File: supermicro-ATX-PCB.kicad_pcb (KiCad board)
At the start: 2 copper layers, 27.9 x 30.5 mm, 6 parts

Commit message: added through hole for female header
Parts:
- removed ATX-FP: Conn_02x05_Odd_Even, Connector_PinSocket_2.54mm:PinSocket_2x05_P2.54mm_Vertical
- added ATX-FP1: Conn_02x05_Odd_Even, Connector_PinSocket_2.54mm:PinSocket_2x05_P2.54mm_Vertical, B.Cu at (104.1, 78.7)
- moved PWR_FAIL 0.38 mm to (122.6, 63.5)
- moved UID 0.38 mm to (122.6, 68.6)
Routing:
- net /PWR_LED+: track 11.2 -> 13.1 mm

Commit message: testing SMD Female
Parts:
- removed PWR_FAIL, UID: Conn_01x02_Pin, Connector_PinHeader_2.54mm:PinHeader_2x01_P2.54mm_Vertical
- added PWR_FAIL1: Conn_01x02_Pin, Connector_PinHeader_2.54mm:PinHeader_2x01_P2.54mm_Vertical, F.Cu at (123.2, 63.5)
- added UID1: Conn_01x02_Pin, Connector_PinHeader_2.54mm:PinHeader_2x01_P2.54mm_Vertical, F.Cu at (123.2, 68.6)
- ATX-FP1: footprint Connector_PinSocket_2.54mm:PinSocket_2x05_P2.54mm_Vertical -> Connector_PinSocket_2.54mm:PinSocket_2x05_P2.54mm_Vertical_SMD
- moved ATX-FP1 5.69 mm to (101.6, 73.7)
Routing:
- net /PWR_BUTT: track 16.3 -> 1.66 mm
- net GND: track 13.8 -> 0.00 mm
- net /PWR_LED+: track 13.1 -> 0.00 mm
- net /RESET_BUTT: track 11.7 -> 0.00 mm
- net /PWR_LED-: track 11.1 -> 0.00 mm
- net /HDD_LED+: track 8.57 -> 0.00 mm
- net /HDD_LED-: track 6.13 -> 0.00 mm
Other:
- board size 27.9 x 30.5 mm -> 29.3 x 30.5 mm

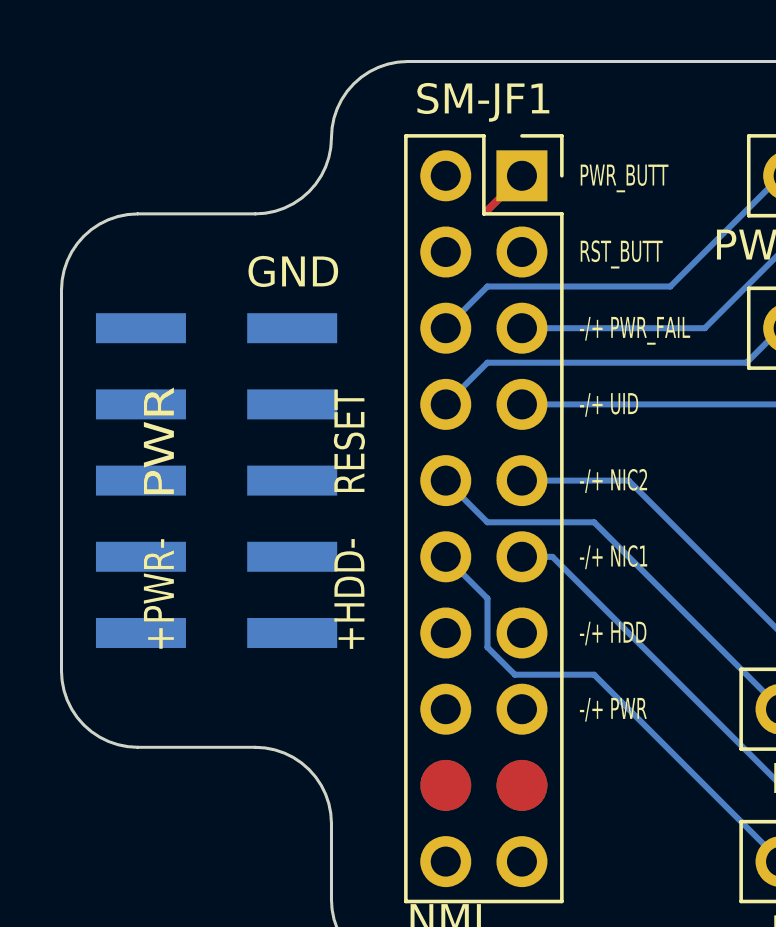
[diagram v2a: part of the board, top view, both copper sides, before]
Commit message: added routing for SMT ATX Female
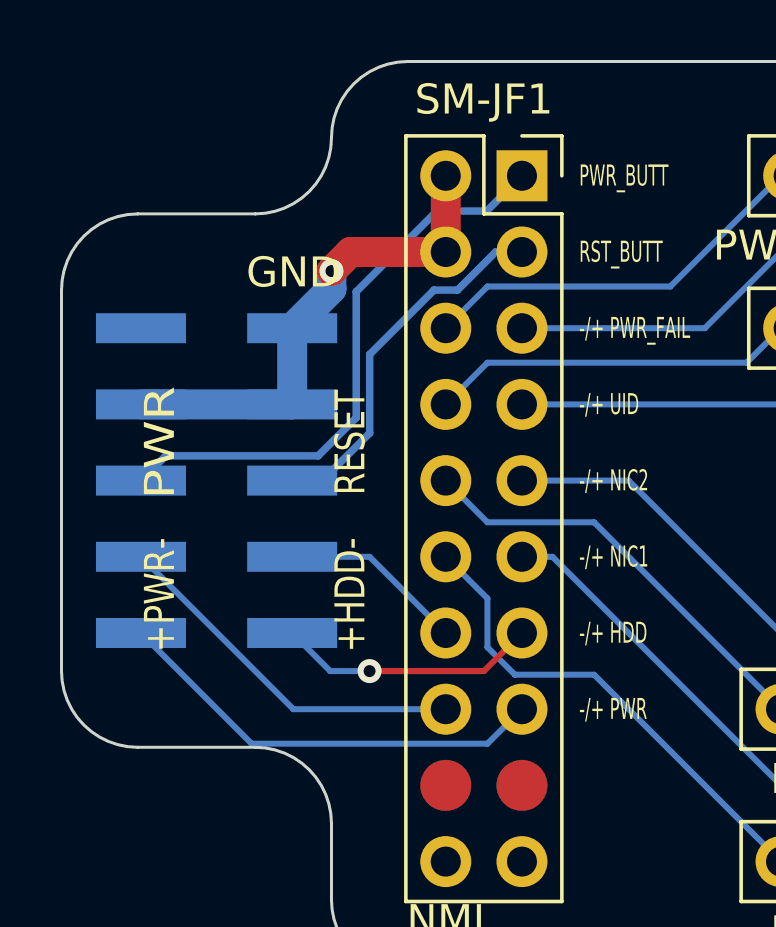
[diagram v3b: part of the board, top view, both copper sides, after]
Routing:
- net /PWR_BUTT: track 1.66 -> 19.4 mm
- net GND: track 0.00 -> 16.6 mm, vias 0 -> 1
- net /PWR_LED+: track 0.00 -> 14.7 mm
- net /RESET_BUTT: track 0.00 -> 12.4 mm
- net /PWR_LED-: track 0.00 -> 12.3 mm
- net /HDD_LED+: track 0.00 -> 8.71 mm, vias 0 -> 1
- net /HDD_LED-: track 0.00 -> 6.17 mm
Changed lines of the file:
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@@
     (effects (font (size 0.7 0.4) (thickness 0.1)) (justify left))
   )
-  (segment (start 111.76 63.5) (end 110.585 64.675) (width 0.25) (layer "F.Cu") (net 6))
+  (segment (start 106.68 80.01) (end 110.49 80.01) (width 0.2) (layer "F.Cu") (net 1))
+  (segment (start 110.49 80.01) (end 111.76 78.74) (width 0.2) (layer "F.Cu") (net 1))
+  (via (at 106.68 80.01) (size 0.8) (drill 0.4) (layers "F.Cu" "B.Cu") (net 1))
+  (segment (start 104.1 78.74) (end 105.37 80.01) (width 0.2) (layer "B.Cu") (net 1))
+  (segment (start 105.37 80.01) (end 106.68 80.01) (width 0.2) (layer "B.Cu") (net 1))
+  (segment (start 110.61 82.43) (end 102.75 82.43) (width 0.2) (layer "B.Cu") (net 2))
+  (segment (start 111.76 81.28) (end 110.61 82.43) (width 0.2) (layer "B.Cu") (net 2))
+  (segment (start 102.75 82.43) (end 99.06 78.74) (width 0.2) (layer "B.Cu") (net 2))
+  (segment (start 104.1 76.2) (end 106.68 76.2) (width 0.2) (layer "B.Cu") (net 3))
+  (segment (start 106.68 76.2) (end 109.22 78.74) (width 0.2) (layer "B.Cu") (net 3))
+  (segment (start 104.14 81.28) (end 99.06 76.2) (width 0.2) (layer "B.Cu") (net 4))
+  (segment (start 109.22 81.28) (end 104.14 81.28) (width 0.2) (layer "B.Cu") (net 4))
+  (segment (start 111.76 66.04) (end 110.881701 66.04) (width 0.25) (layer "B.Cu") (net 5))
+  (segment (start 105.1 73.66) (end 104.1 73.66) (width 0.25) (layer "B.Cu") (net 5))
+  (segment (start 109.611701 67.31) (end 108.828299 67.31) (width 0.25) (layer "B.Cu") (net 5))
+  (segment (start 106.685 69.453299) (end 106.685 72.075) (width 0.25) (layer "B.Cu") (net 5))
+  (segment (start 108.828299 67.31) (end 106.685 69.453299) (width 0.25) (layer "B.Cu") (net 5))
+  (segment (start 106.685 72.075) (end 105.1 73.66) (width 0.25) (layer "B.Cu") (net 5))
+  (segment (start 110.881701 66.04) (end 109.611701 67.31) (width 0.25) (layer "B.Cu") (net 5))
+  (segment (start 104.965 72.835) (end 99.885 72.835) (width 0.25) (layer "B.Cu") (net 6))
+  (segment (start 108.923299 64.675) (end 106.235 67.363299) (width 0.25) (layer "B.Cu") (net 6))
+  (segment (start 110.585 64.675) (end 108.923299 64.675) (width 0.25) (layer "B.Cu") (net 6))
+  (segment (start 106.235 67.363299) (end 106.235 71.565) (width 0.25) (layer "B.Cu") (net 6))
+  (segment (start 99.885 72.835) (end 99.06 73.66) (width 0.25) (layer "B.Cu") (net 6))
+  (segment (start 106.235 71.565) (end 104.965 72.835) (width 0.25) (layer "B.Cu") (net 6))
+  (segment (start 111.76 63.5) (end 110.585 64.675) (width 0.25) (layer "B.Cu") (net 6))
+  (segment (start 109.22 63.5) (end 109.22 66.04) (width 1) (layer "F.Cu") (net 7))
+  (segment (start 106.045 66.04) (end 105.41 66.675) (width 1) (layer "F.Cu") (net 7))
+  (segment (start 109.22 66.04) (end 106.045 66.04) (width 1) (layer "F.Cu") (net 7))
+  (via (at 105.41 66.675) (size 0.8) (drill 0.4) (layers "F.Cu" "B.Cu") (net 7))
+  (segment (start 104.1 71.12) (end 99.06 71.12) (width 1) (layer "B.Cu") (net 7))
+  (segment (start 104.1 68.58) (end 104.1 71.12) (width 1) (layer "B.Cu") (net 7))
+  (segment (start 105.41 67.27) (end 104.1 68.58) (width 1) (layer "B.Cu") (net 7))
+  (segment (start 105.41 66.675) (end 105.41 67.27) (width 1) (layer "B.Cu") (net 7))
   (segment (start 120.396 86.36) (end 114.166 80.13) (width 0.2) (layer "B.Cu") (net 9))
   (segment (start 110.61 79.216346) (end 110.61 77.59) (width 0.2) (layer "B.Cu") (net 9))

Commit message: added THT board
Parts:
- removed PWR_FAIL1, UID1: Conn_01x02_Pin, Connector_PinHeader_2.54mm:PinHeader_2x01_P2.54mm_Vertical
- added PWR_FAIL: Conn_01x02_Pin, Connector_PinHeader_2.54mm:PinHeader_2x01_P2.54mm_Vertical, F.Cu at (122.9, 63.5)
- added UID: Conn_01x02_Pin, Connector_PinHeader_2.54mm:PinHeader_2x01_P2.54mm_Vertical, F.Cu at (122.9, 68.6)
- ATX-FP1: footprint Connector_PinSocket_2.54mm:PinSocket_2x05_P2.54mm_Vertical_SMD -> Connector_PinSocket_2.54mm:PinSocket_2x05_P2.54mm_Vertical
- moved ATX-FP1 5.69 mm to (104.1, 78.7)
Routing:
- net /PWR_BUTT: track 19.4 -> 16.3 mm
- net GND: track 16.6 -> 13.8 mm, vias 1 -> 0
- net /PWR_LED+: track 14.7 -> 13.1 mm
- net /PWR_LED-: track 12.3 -> 11.1 mm
- net /RESET_BUTT: track 12.4 -> 11.7 mm
- net /HDD_LED+: track 8.71 -> 8.57 mm, vias 1 -> 0
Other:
- board size 29.3 x 30.5 mm -> 27.9 x 30.5 mm

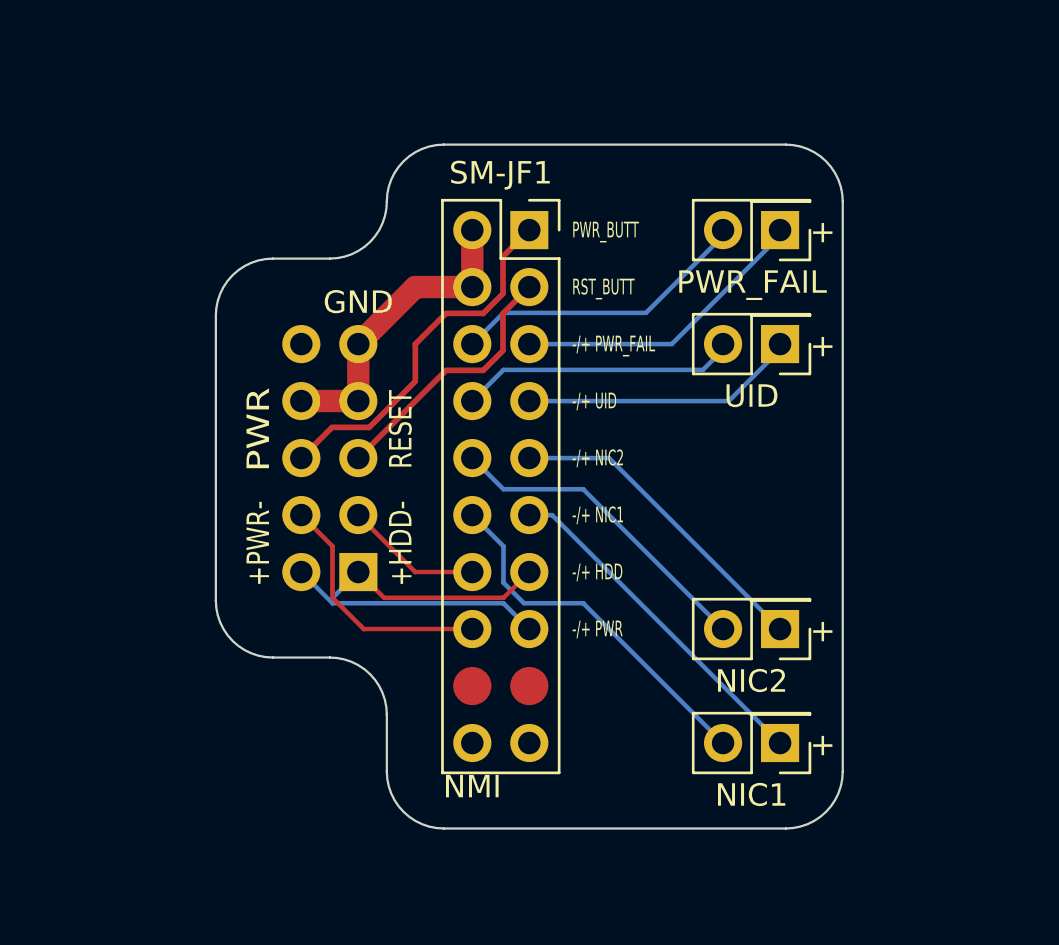
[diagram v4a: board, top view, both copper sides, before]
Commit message: switched polarity of LEDs, isolated all terminals of buttons
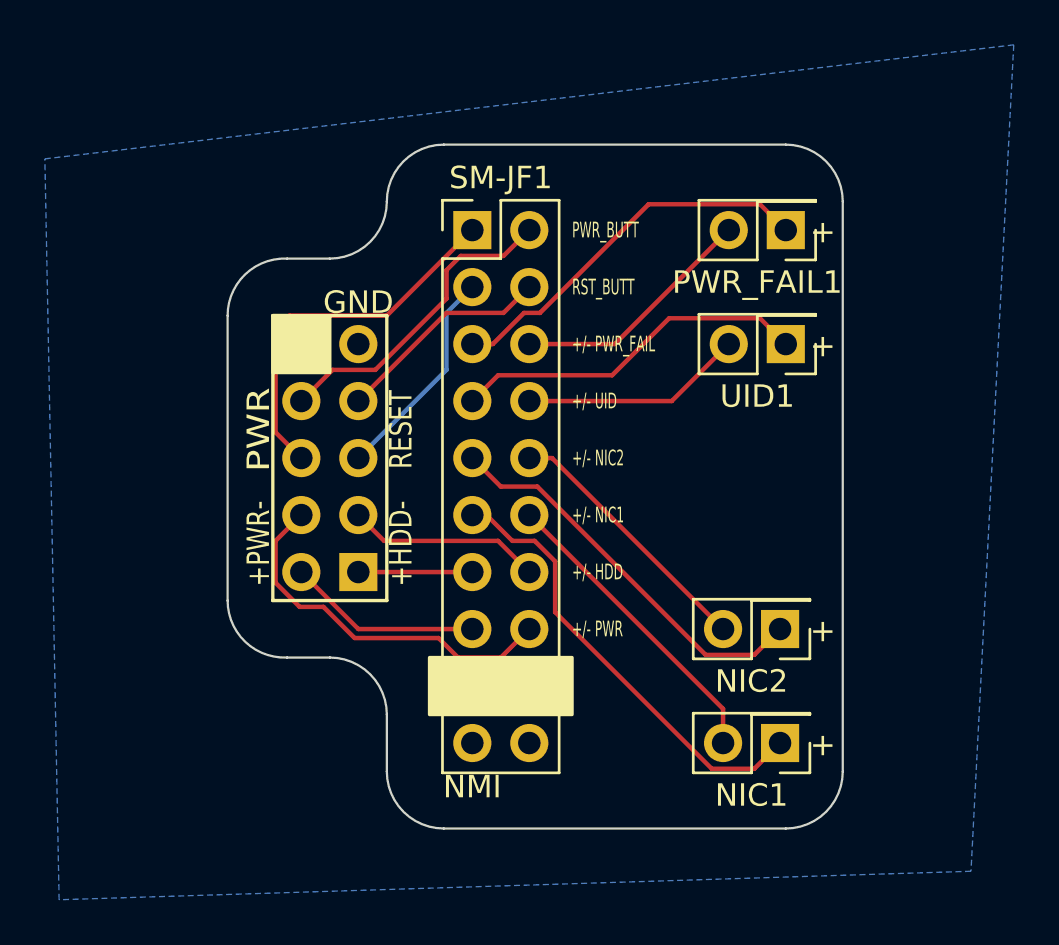
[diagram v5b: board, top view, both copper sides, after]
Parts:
- removed PWR_FAIL, UID: Conn_01x02_Pin, Connector_PinHeader_2.54mm:PinHeader_2x01_P2.54mm_Vertical
- added PWR_FAIL1: Conn_01x02_Pin, Connector_PinHeader_2.54mm:PinHeader_2x01_P2.54mm_Vertical, F.Cu at (123.2, 63.5)
- added UID1: Conn_01x02_Pin, Connector_PinHeader_2.54mm:PinHeader_2x01_P2.54mm_Vertical, F.Cu at (123.2, 68.6)
- SM-JF1: footprint Connector_PinSocket_2.54mm:PinSocket_2x10_P2.54mm_Vertical -> Connector_PinHeader_2.54mm:PinHeader_2x10_P2.54mm_Vertical
- moved SM-JF1 2.54 mm to (109.2, 63.5)
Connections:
- net /PWR_BUTT renamed /PWR_BUTT+
- net /RESET_BUTT renamed /RESET_BUTT+
- ATX-FP1 pad 7: GND -> /RESET_BUTT-
- ATX-FP1 pad 8: GND -> /PWR_BUTT-
- SM-JF1 pad 2: GND -> /PWR_BUTT-
- SM-JF1 pad 4: GND -> /RESET_BUTT-
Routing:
- net /PWR_BUTT-: track 0.00 -> 14.1 mm
- net GND: track 13.8 -> 0.00 mm
- net /RESET_BUTT-: track 0.00 -> 9.72 mm
- net /PWR_LED-: track 11.1 -> 16.7 mm
- net /NIC1_LED+: track 15.4 -> 20.2 mm
- net /PWR_LED+: track 13.1 -> 8.67 mm
- net /NIC2_LED+: track 14.3 -> 17.8 mm
- net /HDD_LED+: track 8.57 -> 5.08 mm
- net /PWR_FAIL_LED+: track 13.5 -> 17.0 mm
- net /UID_LED+: track 12.5 -> 16.0 mm
- net /NIC1_LED-: track 16.3 -> 13.7 mm
- net /UID_LED-: track 12.5 -> 9.94 mm
- net /PWR_FAIL_LED-: track 13.5 -> 11.0 mm
- net /NIC2_LED-: track 14.3 -> 11.8 mm
- net /HDD_LED-: track 6.13 -> 8.67 mm
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- added copper zone on B.Cu, net GND
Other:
- board size 27.9 x 30.5 mm -> 27.4 x 30.5 mm
- board text added: "+/- HDD"
- board text added: "+/- NIC1"
- board text added: "+/- NIC2"
- board text added: "+/- PWR"
- board text added: "+/- PWR_FAIL"
- board text added: "+/- UID"
- board text added: "joanne-lab r1.1"
- board text removed: "-/+ HDD"
- board text removed: "-/+ NIC1"
- board text removed: "-/+ NIC2"
- board text removed: "-/+ PWR"
- board text removed: "-/+ PWR_FAIL"
- board text removed: "-/+ UID"
- board text removed: "joanne-lab r1.0"
